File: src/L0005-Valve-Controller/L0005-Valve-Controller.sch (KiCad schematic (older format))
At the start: 50 parts, among them J1 Jumper_NO, J2 Jumper_NO, P1 3220-20-0200-00, P10 353620650, P11 353620650, P12 353620650, P13 353620650, P14 647676-3, P15 647676-3, P2 140-504-415-000, P9 647676-2, U1 LPC54113J256BD64QL, U2 LMS8117AMP-3.3_NOPB, U3 MAX3370EXK+T, U4 MAX3370EXK+T

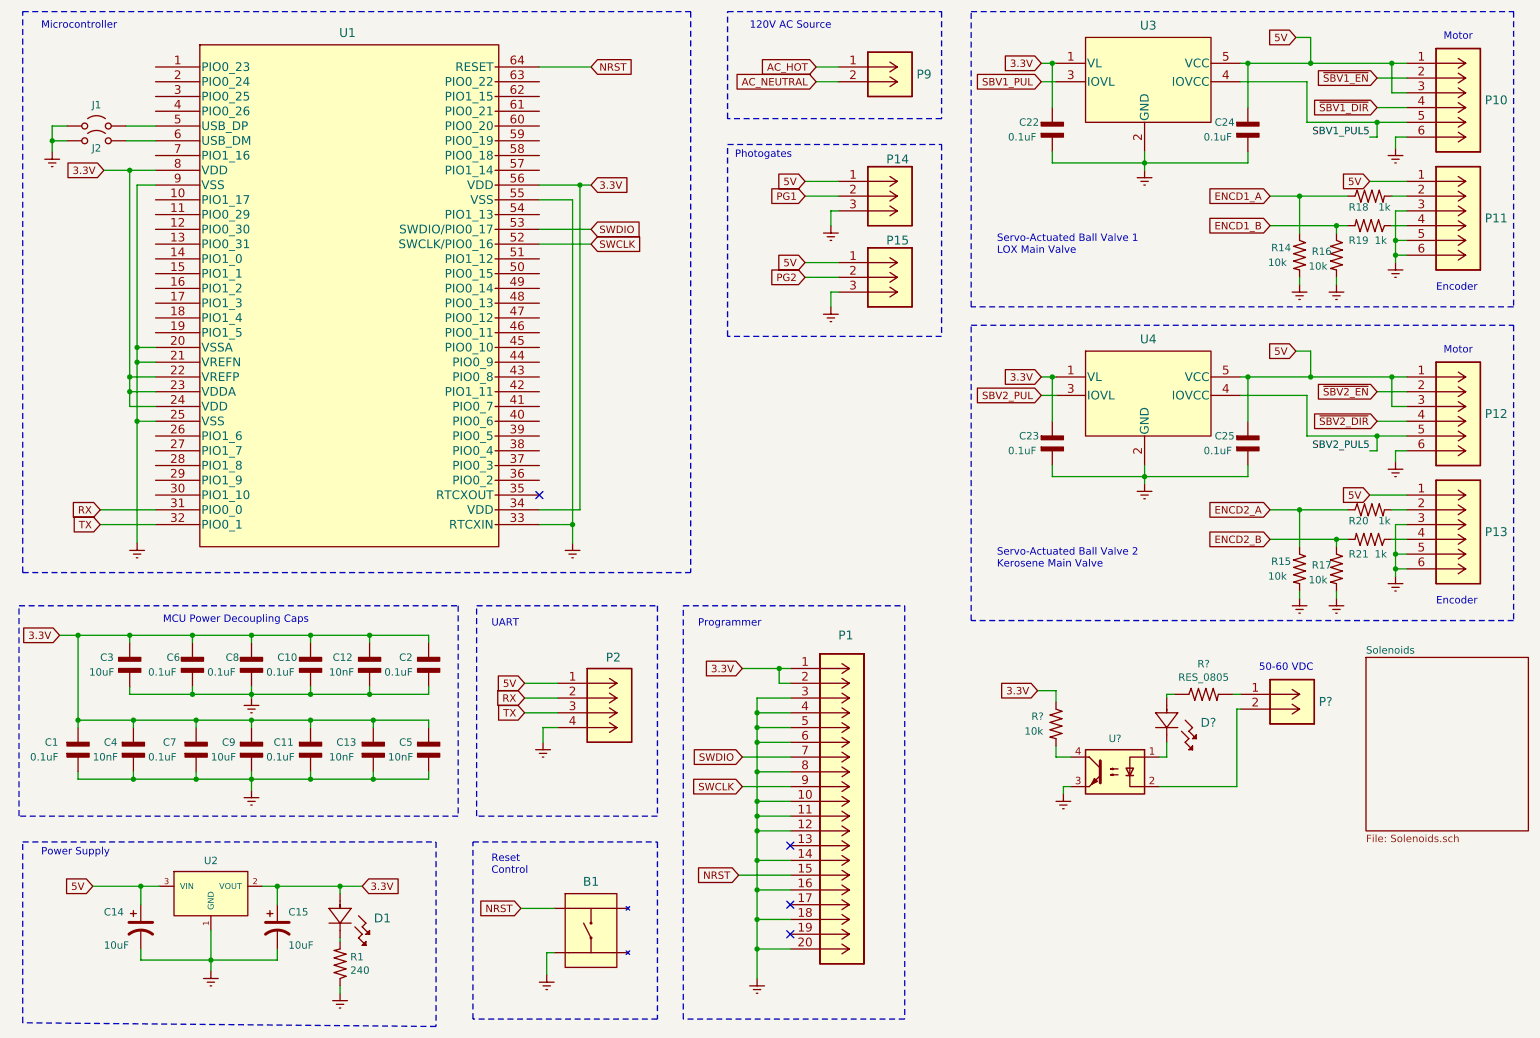
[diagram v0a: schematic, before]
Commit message: Added MCU control signals
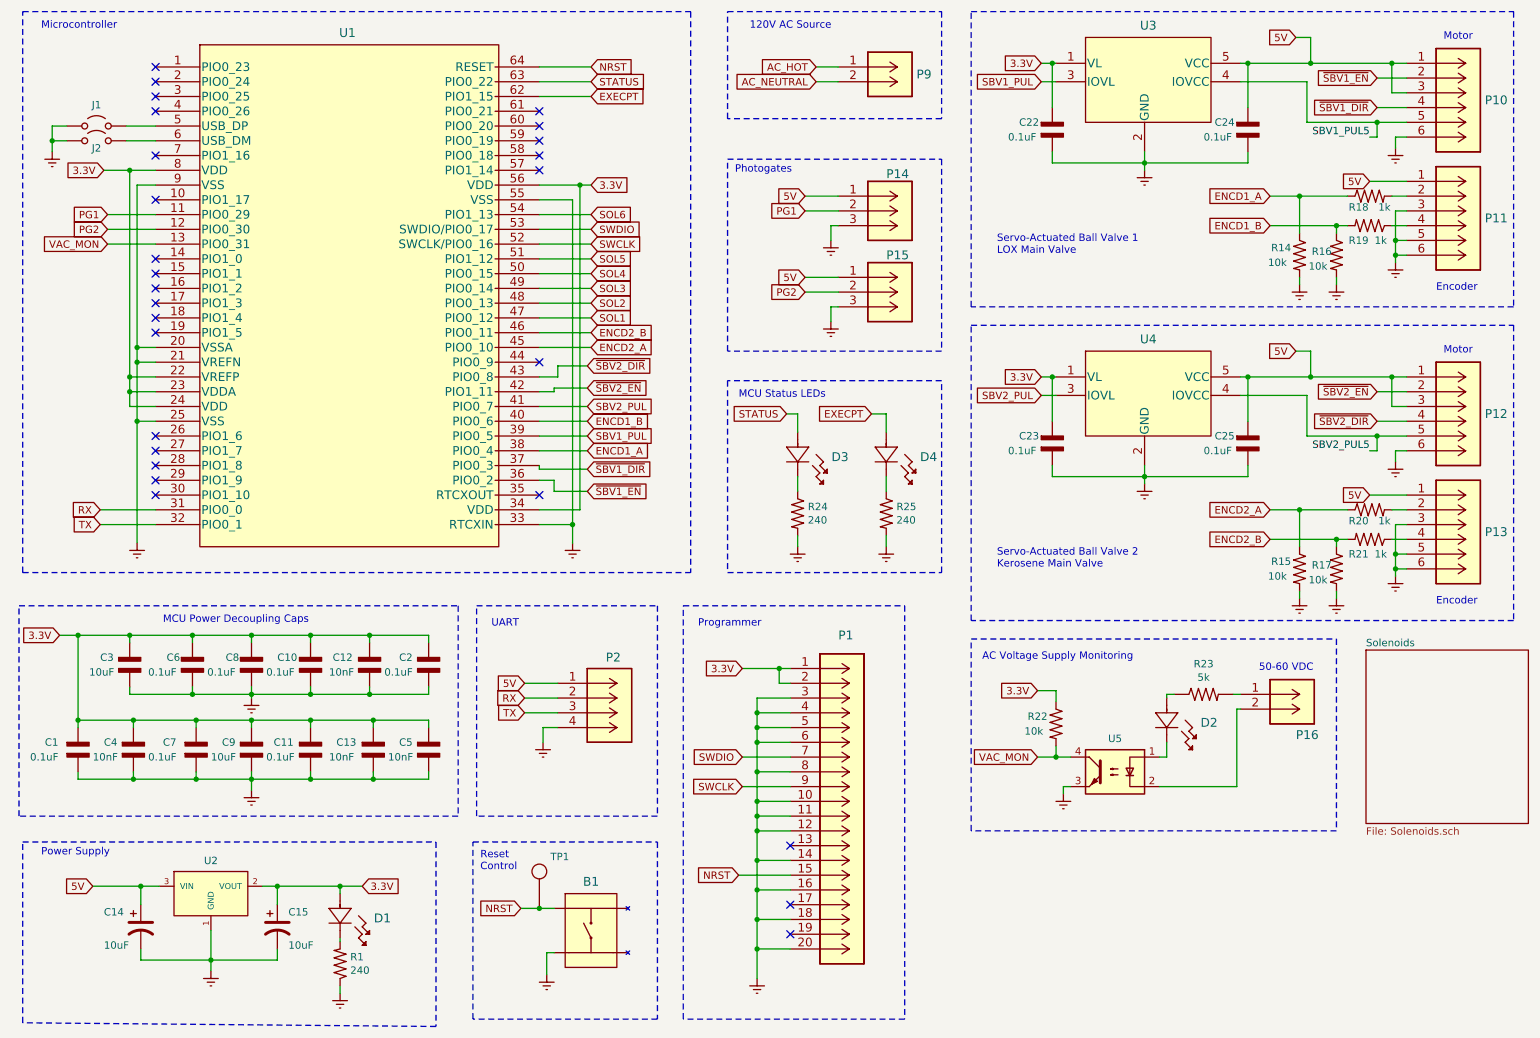
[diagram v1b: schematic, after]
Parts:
- added D3: LED_AMBER, symbol L0005-Valve-Controller:LED_AMBER
- added D4: LED_RED, symbol L0005-Valve-Controller:LED_RED
- added R24, R25: 240, symbol L0005-Valve-Controller:RES_0603
- added TP1: TP, symbol L0005-Valve-Controller:TP
- R23: renamed from R?; value RES_0805 -> 5k
- gave numbers to parts that had none: 4
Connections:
- net ENCD1_A: now also U1.38 (PIO0_4)
- net ENCD1_B: now also U1.40 (PIO0_6)
- net ENCD2_A: now also U1.45 (PIO0_10)
- net ENCD2_B: now also U1.46 (PIO0_11)
- net Earth: now also R24.2, R25.2
- net NRST: now also TP1.1
- net PG1: now also U1.11 (PIO0_29)
- net PG2: now also U1.12 (PIO0_30)
- net SBV1_PUL: now also U1.39 (PIO0_5)
- net SBV2_PUL: now also U1.41 (PIO0_7)
- net ~SBV1_DIR: now also U1.37 (PIO0_3)
- net ~SBV1_EN: now also U1.36 (PIO0_2)
- net ~SBV2_DIR: now also U1.43 (PIO0_8)
- net ~SBV2_EN: now also U1.42 (PIO1_11)
- net VAC_MON: now reaches U1.13 (PIO0_31)
- net VAC_MON: now also R22.2, U5.4
- net SOL1: now reaches U1.47 (PIO0_12)
- net SOL2: now reaches U1.48 (PIO0_13)
- net SOL3: now reaches U1.49 (PIO0_14)
- net SOL4: now reaches U1.50 (PIO0_15)
- net SOL5: now reaches U1.51 (PIO1_12)
- net SOL6: now reaches U1.54 (PIO1_13)
- net EXECPT: now reaches U1.62 (PIO1_15)
- net EXECPT: now also D4.2
- net STATUS: now reaches U1.63 (PIO0_22)
- net STATUS: now also D3.2
- new net: D3.1, R24.1
- new net: D4.1, R25.1
- no-connect marks 4 -> 27
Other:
- note added: "AC Voltage Supply Monitoring"
- note added: "MCU Status LEDs"
- moved on the sheet: P14, P15

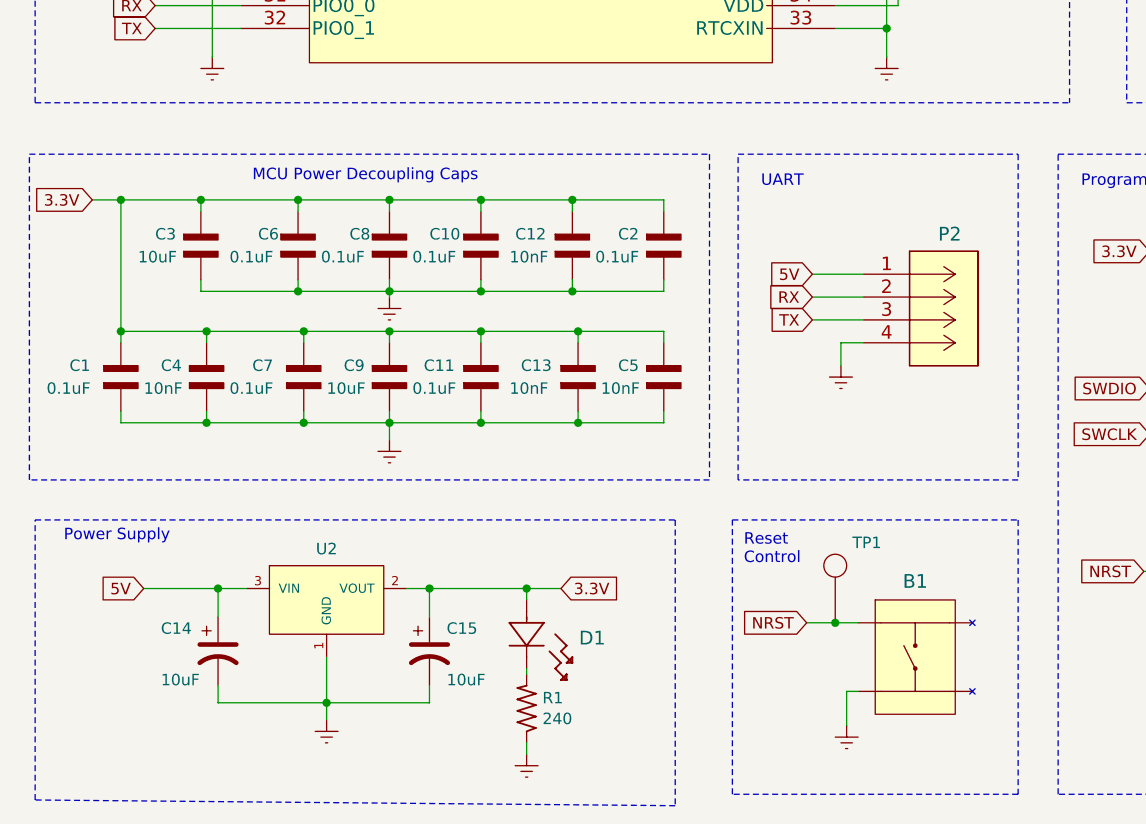
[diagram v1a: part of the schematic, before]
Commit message: Added test points
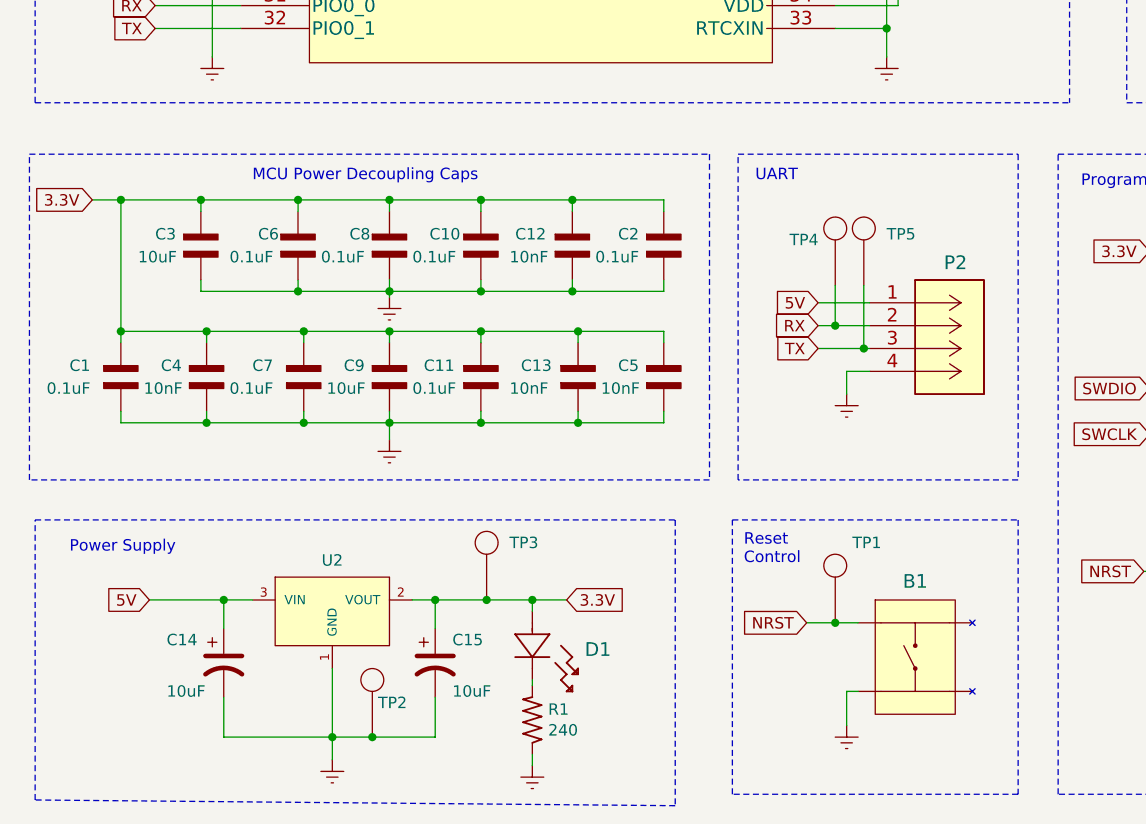
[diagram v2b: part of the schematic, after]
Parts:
- added TP2, TP3, TP4, TP5: TP, symbol L0005-Valve-Controller:TP
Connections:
- net 3.3V: now also TP3.1
- net Earth: now also TP2.1
- net RX: now also TP4.1
- net TX: now also TP5.1
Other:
- moved on the sheet: C14, C15, D1, P2, R1, U2
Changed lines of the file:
@@
 Wire Wire Line
 	4575 1925 4650 1925
-Text GLabel 1275 6675 0    50   Input ~ 0
+Text GLabel 1300 6725 0    50   Input ~ 0
 5V
 $Comp
 L L0005-Valve-Controller:LMS8117AMP-3.3_NOPB U2
 U 1 1 61F98442
-P 2075 6725
-F 0 "U2" H 2075 6948 50  0000 C CNN
-F 1 "LMS8117AMP-3.3_NOPB" H 2075 6949 50  0001 C CNN
-F 2 "" H 2075 6725 50  0001 C CNN
-F 3 "" H 2075 6725 50  0001 C CNN
-	1    2075 6725
-	1    0    0    -1
-$EndComp
-Wire Wire Line
-	1275 6675 1600 6675
+P 2100 6775
+F 0 "U2" H 2100 6998 50  0000 C CNN
+F 1 "LMS8117AMP-3.3_NOPB" H 2100 6999 50  0001 C CNN
+F 2 "" H 2100 6775 50  0001 C CNN
+F 3 "" H 2100 6775 50  0001 C CNN
+	1    2100 6775
+	1    0    0    -1
+$EndComp
+Wire Wire Line
+	1300 6725 1625 6725
 $Comp
 L L0005-Valve-Controller:Earth #PWR03
 U 1 1 61FA1738
-P 2075 7250
-F 0 "#PWR03" H 2075 7000 50  0001 C CNN
-F 1 "Earth" H 2075 7100 50  0001 C CNN
-F 2 "" H 2075 7250 50  0001 C CNN
-F 3 "" H 2075 7250 50  0001 C CNN
-	1    2075 7250
-	1    0    0    -1
-$EndComp
-Wire Wire Line
-	2075 7250 2075 7175
-Text GLabel 3100 6675 2    50   Input ~ 0
+P 2100 7425
+F 0 "#PWR03" H 2100 7175 50  0001 C CNN
+F 1 "Earth" H 2100 7275 50  0001 C CNN
+F 2 "" H 2100 7425 50  0001 C CNN
+F 3 "" H 2100 7425 50  0001 C CNN
+	1    2100 7425
+	1    0    0    -1
+$EndComp
+Wire Wire Line
+	2100 7425 2100 7325
+Text GLabel 3125 6725 2    50   Input ~ 0
 3.3V
 Wire Wire Line
-	2425 6675 2525 6675
+	2450 6725 2550 6725
 $Comp
 L L0005-Valve-Controller:CAP_Polar C14
 U 1 1 61FB83F5
-P 1600 6950
-F 0 "C14" H 1350 7050 50  0000 L CNN
-F 1 "10uF" H 1350 6825 50  0000 L CNN
-F 2 "" H 1600 6950 50  0001 C CNN
-F 3 "~" H 1600 6950 50  0001 C CNN
-	1    1600 6950
-	1    0    0    -1
-$EndComp
-Wire Wire Line
-	1600 6800 1600 6675
-Connection ~ 1600 6675
-Wire Wire Line
-	1600 6675 1725 6675
-Wire Wire Line
-	1600 7100 1600 7175
-Wire Wire Line
-	1600 7175 2075 7175
-Connection ~ 2075 7175
-Wire Wire Line
-	2075 7175 2075 6975
+P 1625 7000
+F 0 "C14" H 1375 7100 50  0000 L CNN
+F 1 "10uF" H 1375 6875 50  0000 L CNN
+F 2 "" H 1625 7000 50  0001 C CNN
+F 3 "~" H 1625 7000 50  0001 C CNN
+	1    1625 7000
+	1    0    0    -1
+$EndComp
+Wire Wire Line
+	1625 6850 1625 6725
+Connection ~ 1625 6725
+Wire Wire Line
+	1625 6725 1750 6725
+Wire Wire Line
+	1625 7150 1625 7325
+Wire Wire Line
+	1625 7325 2100 7325
+Connection ~ 2100 7325
+Wire Wire Line
+	2100 7325 2100 7025
 $Comp
 L L0005-Valve-Controller:CAP_Polar C15
 U 1 1 61FC4D2A
-P 2525 6950
-F 0 "C15" H 2600 7050 50  0000 L CNN
-F 1 "10uF" H 2600 6825 50  0000 L CNN
-F 2 "" H 2525 6950 50  0001 C CNN
-F 3 "~" H 2525 6950 50  0001 C CNN
-	1    2525 6950
-	1    0    0    -1
-$EndComp
-Wire Wire Line
-	2525 6800 2525 6675
-Connection ~ 2525 6675
-Wire Wire Line
-	2525 6675 2950 6675
-Wire Wire Line
-	2075 7175 2525 7175
-Wire Wire Line
-	2525 7175 2525 7100
+P 2550 7000
+F 0 "C15" H 2625 7100 50  0000 L CNN
+F 1 "10uF" H 2625 6875 50  0000 L CNN
+F 2 "" H 2550 7000 50  0001 C CNN
+F 3 "~" H 2550 7000 50  0001 C CNN
+	1    2550 7000
+	1    0    0    -1
+$EndComp
+Wire Wire Line
+	2550 6850 2550 6725
+Connection ~ 2550 6725
+Wire Wire Line
+	2550 6725 2775 6725
+Wire Wire Line
+	2100 7325 2275 7325
+Wire Wire Line
+	2550 7325 2550 7150
 $Comp
 L L0005-Valve-Controller:LED_GREEN D1
 U 1 1 61FE6C7C
-P 2950 6925
-F 0 "D1" H 3179 6958 60  0000 L CNN
-F 1 "LED_GREEN" H 3178 6905 60  0001 L CNN
-F 2 "" H 3150 6565 60  0001 C CNN
-F 3 "" V 2950 7175 60  0000 C CNN
-	1    2950 6925
-	1    0    0    -1
-$EndComp
-Wire Wire Line
-	2950 6725 2950 6675
-Connection ~ 2950 6675
-Wire Wire Line
-	2950 6675 3100 6675
+P 2975 6975
+F 0 "D1" H 3204 7008 60  0000 L CNN
+F 1 "LED_GREEN" H 3203 6955 60  0001 L CNN
+F 2 "" H 3175 6615 60  0001 C CNN
+F 3 "" V 2975 7225 60  0000 C CNN
+	1    2975 6975
+	1    0    0    -1
+$EndComp
+Wire Wire Line
+	2975 6775 2975 6725
+Connection ~ 2975 6725
+Wire Wire Line
+	2975 6725 3125 6725
 $Comp
 L L0005-Valve-Controller:RES_0603 R1
 U 1 1 61FED053
-P 2950 7200
-F 0 "R1" V 2996 7269 50  0000 L CNN
-F 1 "240" V 2905 7269 50  0000 L CNN
-F 2 "" H 3000 6700 50  0001 L BNN
-F 3 "" H 2950 7200 50  0001 L BNN
-	1    2950 7200
+P 2975 7250
+F 0 "R1" V 3021 7319 50  0000 L CNN
+F 1 "240" V 2930 7319 50  0000 L CNN
+F 2 "" H 3025 6750 50  0001 L BNN
+F 3 "" H 2975 7250 50  0001 L BNN
+	1    2975 7250
 	0    1    -1   0
 $EndComp
 Wire Wire Line
-	2950 7050 2950 7025
+	2975 7100 2975 7075
 $Comp
 L L0005-Valve-Controller:Earth #PWR04
 U 1 1 61FF6A19
-P 2950 7400
-F 0 "#PWR04" H 2950 7150 50  0001 C CNN
-F 1 "Earth" H 2950 7250 50  0001 C CNN
-F 2 "" H 2950 7400 50  0001 C CNN
-F 3 "" H 2950 7400 50  0001 C CNN
-	1    2950 7400
-	1    0    0    -1
-$EndComp
-Wire Wire Line
-	2950 7400 2950 7350
-Text Notes 925  6475 0    50   ~ 0
+P 2975 7450
+F 0 "#PWR04" H 2975 7200 50  0001 C CNN
+F 1 "Earth" H 2975 7300 50  0001 C CNN
+F 2 "" H 2975 7450 50  0001 C CNN
+F 3 "" H 2975 7450 50  0001 C CNN
+	1    2975 7450
+	1    0    0    -1
+$EndComp
+Wire Wire Line
+	2975 7450 2975 7400
+Text Notes 950  6525 0    50   ~ 0
 Power Supply
 Wire Notes Line
@@
 L L0005-Valve-Controller:140-504-415-000 P2
 U 1 1 622DBA6B
-P 4425 5300
-F 0 "P2" H 4750 5475 60  0000 L CNN
-F 1 "140-504-415-000" H 4775 4850 60  0001 C CNN
-F 2 "CONN_4840.2201_SCH" H 4825 4700 60  0001 C CNN
-F 3 "" H 4425 5300 60  0000 C CNN
-	1    4425 5300
-	1    0    0    -1
-$EndComp
-Text GLabel 4200 5300 0    50   Input ~ 0
+P 4450 5425
+F 0 "P2" H 4775 5600 60  0000 L CNN
+F 1 "140-504-415-000" H 4800 4975 60  0001 C CNN
+F 2 "CONN_4840.2201_SCH" H 4850 4825 60  0001 C CNN
+F 3 "" H 4450 5425 60  0000 C CNN
+	1    4450 5425
+	1    0    0    -1
+$EndComp
+Text GLabel 4225 5425 0    50   Input ~ 0
 5V
 Wire Wire Line
-	4200 5300 4425 5300
+	4225 5425 4450 5425
 $Comp
 L L0005-Valve-Controller:Earth #PWR010
 U 1 1 622F0D80
-P 4325 5700
-F 0 "#PWR010" H 4325 5450 50  0001 C CNN
-F 1 "Earth" H 4325 5550 50  0001 C CNN
-F 2 "" H 4325 5700 50  0001 C CNN
-F 3 "" H 4325 5700 50  0001 C CNN
-	1    4325 5700
-	1    0    0    -1
-$EndComp
-Wire Wire Line
-	4325 5700 4325 5600
-Wire Wire Line
-	4325 5600 4425 5600
-Text GLabel 4200 5400 0    50   Input ~ 0
+P 4350 5825
+F 0 "#PWR010" H 4350 5575 50  0001 C CNN
+F 1 "Earth" H 4350 5675 50  0001 C CNN
+F 2 "" H 4350 5825 50  0001 C CNN
+F 3 "" H 4350 5825 50  0001 C CNN
+	1    4350 5825
+	1    0    0    -1
+$EndComp
+Wire Wire Line
+	4350 5825 4350 5725
+Wire Wire Line
+	4350 5725 4450 5725
+Text GLabel 4225 5525 0    50   Input ~ 0
 RX
 Wire Wire Line
-	4200 5400 4425 5400
-Text GLabel 4200 5500 0    50   Input ~ 0
+	4225 5525 4300 5525
+Text GLabel 4225 5625 0    50   Input ~ 0
 TX
 Wire Wire Line
-	4200 5500 4425 5500
+	4225 5625 4425 5625
 Wire Notes Line
 	5100 4775 5100 6200
@@
 Wire Notes Line
 	3875 4775 5100 4775
-Text Notes 3975 4925 0    50   ~ 0
+Text Notes 3950 4900 0    50   ~ 0
 UART
 Text GLabel 1325 4125 0    50   Input ~ 0
@@
 Wire Wire Line
 	4300 6825 4400 6825
+$Comp
+L L0005-Valve-Controller:TP TP2
+U 1 1 6288896D
+P 2275 7325
+F 0 "TP2" H 2300 7475 50  0000 L CNN
+F 1 "TP" H 2275 7675 50  0001 C CNN
+F 2 "" H 2275 7325 50  0001 C CNN
+F 3 "" H 2275 7325 50  0001 C CNN
+	1    2275 7325
+	1    0    0    -1
+$EndComp
+Connection ~ 2275 7325
+Wire Wire Line
+	2275 7325 2550 7325
+$Comp
+L L0005-Valve-Controller:TP TP3
+U 1 1 629245AD
+P 2775 6725
+F 0 "TP3" H 2875 6975 50  0000 L CNN
+F 1 "TP" H 2775 7075 50  0001 C CNN
+F 2 "" H 2775 6725 50  0001 C CNN
+F 3 "" H 2775 6725 50  0001 C CNN
+	1    2775 6725
+	1    0    0    -1
+$EndComp
+Connection ~ 2775 6725
+Wire Wire Line
+	2775 6725 2975 6725
+$Comp
+L L0005-Valve-Controller:TP TP4
+U 1 1 6296175D
+P 4300 5350
+F 0 "TP4" H 4100 5550 50  0000 L CNN
+F 1 "TP" H 4300 5700 50  0001 C CNN
+F 2 "" H 4300 5350 50  0001 C CNN
+F 3 "" H 4300 5350 50  0001 C CNN
+	1    4300 5350
+	1    0    0    -1
+$EndComp
+$Comp
+L L0005-Valve-Controller:TP TP5
+U 1 1 629652D5
+P 4425 5350
+F 0 "TP5" H 4525 5575 50  0000 L CNN
+F 1 "TP" H 4425 5700 50  0001 C CNN
+F 2 "" H 4425 5350 50  0001 C CNN
+F 3 "" H 4425 5350 50  0001 C CNN
+	1    4425 5350
+	1    0    0    -1
+$EndComp
+Wire Wire Line
+	4300 5350 4300 5525
+Connection ~ 4300 5525
+Wire Wire Line
+	4300 5525 4450 5525
+Wire Wire Line
+	4425 5350 4425 5625
+Connection ~ 4425 5625
+Wire Wire Line
+	4425 5625 4450 5625
 $EndSCHEMATC
